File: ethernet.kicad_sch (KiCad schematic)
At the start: 57 parts, among them J4 Bus_RJ45_7499111121A, U9 KSZ9031RNXCA, Y1 Oscillator_SMD_25MHz_KX-7

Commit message: [#65754] Rev 2.0.0 Initial commit - source design files from so-dimm-ddr5-tester e0a54f86
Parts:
- removed C129: C_100n_16V_0402, data-center-rdimm-ddr5-tester-footprints:C_0402_1005Metric, symbol data-center-rdimm-ddr5-tester:C_100n_16V_0402
- removed C146, C147: C_22p_0402, data-center-rdimm-ddr5-tester-footprints:C_0402_1005Metric, symbol data-center-rdimm-ddr5-tester:C_22p_0402
- removed FB1, FB2, FB3, FB4: FB_120Z_2A_0603, data-center-rdimm-ddr5-tester-footprints:FB_0603_1608Metric, symbol data-center-rdimm-ddr5-tester:FB_120Z_2A_Murata-BLM18PG_0603
- removed J4: Bus_RJ45_7499111121A, data-center-rdimm-ddr5-tester-footprints:RJ45_7499111121A_Horizontal, symbol data-center-rdimm-ddr5-tester:Bus_RJ45_7499111121A
- removed R62, R63, R64, R65, R66, R67, R68, R69, R70, R72: R_10k2_0402, data-center-rdimm-ddr5-tester-footprints:R_0402_1005Metric, symbol data-center-rdimm-ddr5-tester:R_10k2_0402
- removed Y1: Oscillator_SMD_25MHz_KX-7, data-center-rdimm-ddr5-tester-footprints:Oscillator_SMD_Geyer_KX-7-4Pin_3.2x2.5mm, symbol data-center-rdimm-ddr5-tester:Oscillator_SMD_25MHz_KX-7
- added C135, C137, C157, C160, C161, C234: C_100n_0402, antmicro-footprints:C_0402_1005Metric, symbol antmicroCapacitors0402:C_100n_0402
- added C162, C163: C_18p_0402, antmicro-footprints:C_0402_1005Metric, symbol antmicroCapacitors0402:C_18p_0402
- added FB4, FB5, FB6: FB_120Z_2A_Murata-BLM18PG_0603, antmicro-footprints:FB_0603_1608Metric, symbol antmicroFerriteBeadsandChips:FB_120Z_2A_Murata-BLM18PG_0603
- added J6: Bus_RJ45_5-2337992-8, antmicro-footprints:RJ45_X-2337992-8_Horizontal, symbol antmicroModularConnectorsJacksWithMagnetics:Bus_RJ45_5-2337992-8
- added R101, R102, R103, R104, R105, R106, R107, R108, R109, R111: R_10k_0402, antmicro-footprints:R_0402_1005Metric, symbol antmicroResistors0402:R_10k_0402
- added R193: R_330R_0402, antmicro-footprints:R_0402_1005Metric, symbol antmicroResistors0402:R_330R_0402
- added Y2: Resonator_25MHz_ABM8G, antmicro-footprints:Resonator_SMD_Abracon_ABM8G_3.2x2.5mm, symbol antmicroResonators:Resonator_25MHz_ABM8G
- C134: renamed from C127; footprint data-center-rdimm-ddr5-tester-footprints:C_0402_1005Metric -> antmicro-footprints:C_0402_1005Metric; symbol data-center-rdimm-ddr5-tester:C_4u7_0402 -> antmicroCapacitors0402:C_4u7_0402
- C136: renamed from C143; footprint data-center-rdimm-ddr5-tester-footprints:C_0402_1005Metric -> antmicro-footprints:C_0402_1005Metric; symbol data-center-rdimm-ddr5-tester:C_10n_0402 -> antmicroCapacitors0402:C_10n_0402
- C138: renamed from C132; footprint data-center-rdimm-ddr5-tester-footprints:C_0402_1005Metric -> antmicro-footprints:C_0402_1005Metric; symbol data-center-rdimm-ddr5-tester:C_470n_0402 -> antmicroCapacitors0402:C_470n_0402
- C139: renamed from C122; footprint data-center-rdimm-ddr5-tester-footprints:C_0402_1005Metric -> antmicro-footprints:C_0402_1005Metric; symbol data-center-rdimm-ddr5-tester:C_4u7_0402 -> antmicroCapacitors0402:C_4u7_0402
- C140: footprint data-center-rdimm-ddr5-tester-footprints:C_0402_1005Metric -> antmicro-footprints:C_0402_1005Metric; symbol data-center-rdimm-ddr5-tester:C_10n_0402 -> antmicroCapacitors0402:C_10n_0402
- C141: renamed from C137; footprint data-center-rdimm-ddr5-tester-footprints:C_0402_1005Metric -> antmicro-footprints:C_0402_1005Metric; symbol data-center-rdimm-ddr5-tester:C_10n_0402 -> antmicroCapacitors0402:C_10n_0402
- C142: renamed from C123; footprint data-center-rdimm-ddr5-tester-footprints:C_0402_1005Metric -> antmicro-footprints:C_0402_1005Metric; symbol data-center-rdimm-ddr5-tester:C_470n_0402 -> antmicroCapacitors0402:C_470n_0402
- C143: renamed from C136; footprint data-center-rdimm-ddr5-tester-footprints:C_0402_1005Metric -> antmicro-footprints:C_0402_1005Metric; symbol data-center-rdimm-ddr5-tester:C_470n_0402 -> antmicroCapacitors0402:C_470n_0402
- C144: renamed from C141; footprint data-center-rdimm-ddr5-tester-footprints:C_0402_1005Metric -> antmicro-footprints:C_0402_1005Metric; symbol data-center-rdimm-ddr5-tester:C_10n_0402 -> antmicroCapacitors0402:C_10n_0402
- C145: renamed from C124; footprint data-center-rdimm-ddr5-tester-footprints:C_0402_1005Metric -> antmicro-footprints:C_0402_1005Metric; symbol data-center-rdimm-ddr5-tester:C_470n_0402 -> antmicroCapacitors0402:C_470n_0402
- C146: renamed from C131; footprint data-center-rdimm-ddr5-tester-footprints:C_0402_1005Metric -> antmicro-footprints:C_0402_1005Metric; symbol data-center-rdimm-ddr5-tester:C_4u7_0402 -> antmicroCapacitors0402:C_4u7_0402
- C147: renamed from C144; footprint data-center-rdimm-ddr5-tester-footprints:C_0402_1005Metric -> antmicro-footprints:C_0402_1005Metric; symbol data-center-rdimm-ddr5-tester:C_10n_0402 -> antmicroCapacitors0402:C_10n_0402
- C148: renamed from C126; footprint data-center-rdimm-ddr5-tester-footprints:C_0402_1005Metric -> antmicro-footprints:C_0402_1005Metric; symbol data-center-rdimm-ddr5-tester:C_470n_0402 -> antmicroCapacitors0402:C_470n_0402
- C149: renamed from C130; footprint data-center-rdimm-ddr5-tester-footprints:C_0402_1005Metric -> antmicro-footprints:C_0402_1005Metric; symbol data-center-rdimm-ddr5-tester:C_470n_0402 -> antmicroCapacitors0402:C_470n_0402
- C150: renamed from C135; footprint data-center-rdimm-ddr5-tester-footprints:C_0402_1005Metric -> antmicro-footprints:C_0402_1005Metric; symbol data-center-rdimm-ddr5-tester:C_10n_0402 -> antmicroCapacitors0402:C_10n_0402
- C151: renamed from C139; footprint data-center-rdimm-ddr5-tester-footprints:C_0402_1005Metric -> antmicro-footprints:C_0402_1005Metric; symbol data-center-rdimm-ddr5-tester:C_10n_0402 -> antmicroCapacitors0402:C_10n_0402
- C152: renamed from C128; footprint data-center-rdimm-ddr5-tester-footprints:C_0402_1005Metric -> antmicro-footprints:C_0402_1005Metric; symbol data-center-rdimm-ddr5-tester:C_4u7_0402 -> antmicroCapacitors0402:C_4u7_0402
- C153: renamed from C142; footprint data-center-rdimm-ddr5-tester-footprints:C_0402_1005Metric -> antmicro-footprints:C_0402_1005Metric; symbol data-center-rdimm-ddr5-tester:C_10n_0402 -> antmicroCapacitors0402:C_10n_0402
- C154: renamed from C134; footprint data-center-rdimm-ddr5-tester-footprints:C_0402_1005Metric -> antmicro-footprints:C_0402_1005Metric; symbol data-center-rdimm-ddr5-tester:C_10n_0402 -> antmicroCapacitors0402:C_10n_0402
- C155: renamed from C133; footprint data-center-rdimm-ddr5-tester-footprints:C_0402_1005Metric -> antmicro-footprints:C_0402_1005Metric; symbol data-center-rdimm-ddr5-tester:C_4u7_0402 -> antmicroCapacitors0402:C_4u7_0402
- C156: renamed from C145; footprint data-center-rdimm-ddr5-tester-footprints:C_0402_1005Metric -> antmicro-footprints:C_0402_1005Metric; symbol data-center-rdimm-ddr5-tester:C_10n_0402 -> antmicroCapacitors0402:C_10n_0402
- C158: renamed from C138; footprint data-center-rdimm-ddr5-tester-footprints:C_0402_1005Metric -> antmicro-footprints:C_0402_1005Metric; symbol data-center-rdimm-ddr5-tester:C_4u7_0402 -> antmicroCapacitors0402:C_4u7_0402
- C159: renamed from C125; footprint data-center-rdimm-ddr5-tester-footprints:C_0402_1005Metric -> antmicro-footprints:C_0402_1005Metric; symbol data-center-rdimm-ddr5-tester:C_4u7_0402 -> antmicroCapacitors0402:C_4u7_0402
- R100: renamed from R61; footprint data-center-rdimm-ddr5-tester-footprints:R_0402_1005Metric -> antmicro-footprints:R_0402_1005Metric; symbol data-center-rdimm-ddr5-tester:R_1M8_0402 -> antmicroResistors0402:R_1M8_0402
- R110: renamed from R71; footprint data-center-rdimm-ddr5-tester-footprints:R_0402_1005Metric -> antmicro-footprints:R_0402_1005Metric; symbol data-center-rdimm-ddr5-tester:R_1k_0402 -> antmicroResistors0402:R_1k_0402
- R112: renamed from R59; footprint data-center-rdimm-ddr5-tester-footprints:R_0402_1005Metric -> antmicro-footprints:R_0402_1005Metric; symbol data-center-rdimm-ddr5-tester:R_12k1_0402 -> antmicroResistors0402:R_12k1_0402
- R113: renamed from R73; footprint data-center-rdimm-ddr5-tester-footprints:R_0402_1005Metric -> antmicro-footprints:R_0402_1005Metric; symbol data-center-rdimm-ddr5-tester:R_2k2_0402 -> antmicroResistors0402:R_2k2_0402
- R114: renamed from R74; footprint data-center-rdimm-ddr5-tester-footprints:R_0402_1005Metric -> antmicro-footprints:R_0402_1005Metric; symbol data-center-rdimm-ddr5-tester:R_2k2_0402 -> antmicroResistors0402:R_2k2_0402
- R115: renamed from R75; footprint data-center-rdimm-ddr5-tester-footprints:R_0402_1005Metric -> antmicro-footprints:R_0402_1005Metric; symbol data-center-rdimm-ddr5-tester:R_2k2_0402 -> antmicroResistors0402:R_2k2_0402
- R116: renamed from R76; footprint data-center-rdimm-ddr5-tester-footprints:R_0402_1005Metric -> antmicro-footprints:R_0402_1005Metric; symbol data-center-rdimm-ddr5-tester:R_2k2_0402 -> antmicroResistors0402:R_2k2_0402
- R117: renamed from R77; footprint data-center-rdimm-ddr5-tester-footprints:R_0402_1005Metric -> antmicro-footprints:R_0402_1005Metric; symbol data-center-rdimm-ddr5-tester:R_2k2_0402 -> antmicroResistors0402:R_2k2_0402
- R118: renamed from R78; footprint data-center-rdimm-ddr5-tester-footprints:R_0402_1005Metric -> antmicro-footprints:R_0402_1005Metric; symbol data-center-rdimm-ddr5-tester:R_2k2_0402 -> antmicroResistors0402:R_2k2_0402
- R119: renamed from R79; footprint data-center-rdimm-ddr5-tester-footprints:R_0402_1005Metric -> antmicro-footprints:R_0402_1005Metric; symbol data-center-rdimm-ddr5-tester:R_2k2_0402 -> antmicroResistors0402:R_2k2_0402
- R120: renamed from R80; footprint data-center-rdimm-ddr5-tester-footprints:R_0402_1005Metric -> antmicro-footprints:R_0402_1005Metric; symbol data-center-rdimm-ddr5-tester:R_2k2_0402 -> antmicroResistors0402:R_2k2_0402
- R121: renamed from R81; footprint data-center-rdimm-ddr5-tester-footprints:R_0402_1005Metric -> antmicro-footprints:R_0402_1005Metric; symbol data-center-rdimm-ddr5-tester:R_2k2_0402 -> antmicroResistors0402:R_2k2_0402
- R98: renamed from R58; footprint data-center-rdimm-ddr5-tester-footprints:R_0402_1005Metric -> antmicro-footprints:R_0402_1005Metric; symbol data-center-rdimm-ddr5-tester:R_220R_0402 -> antmicroResistors0402:R_220R_0402
- R99: renamed from R60; footprint data-center-rdimm-ddr5-tester-footprints:R_0402_1005Metric -> antmicro-footprints:R_0402_1005Metric; symbol data-center-rdimm-ddr5-tester:R_220R_0402 -> antmicroResistors0402:R_220R_0402
- U15: renamed from U9; footprint data-center-rdimm-ddr5-tester-footprints:QFN-48-1EP_7x7x0.9mm_P0.5mm_EP3.5x3.5mm -> antmicro-footprints:QFN-48-1EP_7x7x0.9mm_P0.5mm_EP3.5x3.5mm; symbol data-center-rdimm-ddr5-tester:KSZ9031RNXCA -> antmicroInterfaceControllers:KSZ9031RNXCA
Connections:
- net AVDDH: now also FB5.2
- net AVDDL: now also FB4.2
- net AVDDL_PLL: now also C157.2, FB6.2
- net ETH1_N: now also J6.2 (P2)
- net ETH1_P: now also J6.1 (P1)
- net ETH2_N: now also J6.6 (P6)
- net ETH2_P: now also J6.3 (P3)
- net ETH3_N: now also J6.8 (P8)
- net ETH3_P: now also J6.7 (P7)
- net ETH4_N: now also J6.10 (P10)
- net ETH4_P: now also J6.9 (P9)
- net GND: now also R112.1, C135.1, C137.1, C157.1, C160.1, C161.1, C162.1, C163.1, C234.2, R193.1, Y2.2 (SH), Y2.4 (SH); no longer R112.2
- net LED_LINK: now also J6.18 (LED_YEL-), R109.1
- net LED_SPD: now also J6.16 (LED_GRN-), R108.1
- net at R100.1, U15.45 (XO): now also C163.2, Y2.1
- net at R100.2, U15.46 (XI): now also C162.2, Y2.3
- net at U15.48 (ISET): now also R112.2; no longer R112.1
- net at R98.1: now also J6.17 (LED_YEL+)
- net at R99.1: now also J6.15 (LED_GRN+)
- net 1V2_SYS renamed +1V2
- net +1V2: now also FB4.1, FB6.1
- net 3V3_SYS renamed +3V3
- net +3V3: now also C160.2, C161.2, FB5.1, R101.2, R102.2, R103.2, R104.2, R105.2, R106.2, R107.2, R108.2, R109.2, R111.2
- net ETH_INT_N renamed ETH.~{INT}
- net ETH_MDC renamed ETH.MDC
- net ETH_MDIO renamed ETH.MDIO
- net ETH_REF_CLK renamed ETH.REF_CLK
- net ETH.REF_CLK: now also R107.1
- net ETH_RSTN renamed ETH.~{RESET}
- net ETH.~{RESET}: now also R111.1
- net ETH_RXD0 renamed ETH.RXD0
- net ETH.RXD0: now also R101.1
- net ETH_RXD1 renamed ETH.RXD1
- net ETH.RXD1: now also R102.1
- net ETH_RXD2 renamed ETH.RXD2
- net ETH.RXD2: now also R103.1
- net ETH_RXD3 renamed ETH.RXD3
- net ETH.RXD3: now also R104.1
- net ETH_RX_CLK renamed ETH.RXC
- net ETH.RXC: now also R106.1
- net ETH_RX_DV renamed ETH.RX_CTL
- net ETH.RX_CTL: now also R105.1
- net ETH_TXD0 renamed ETH.TXD0
- net ETH_TXD1 renamed ETH.TXD1
- net ETH_TXD2 renamed ETH.TXD2
- net ETH_TXD3 renamed ETH.TXD3
- net ETH_TX_CLK renamed ETH.TXC
- net ETH_TX_EN renamed ETH.TX_CTL
- new net: C135.2, J6.4 (P4)
- new net: C137.2, J6.5 (P5)
- new net: C234.1, J6.19 (SHIELD), J6.20 (SHIELD), R193.2
- no-connect marks 2 -> 5
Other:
- note added: "Bootstrap configuration"
- note added: "CLK125_EN"
- note added: "Gigabit Ethernet"
- note added: "LED_MODE"
- note added: "MODE0"
- note added: "MODE1"
- note added: "MODE2"
- note added: "MODE3"
- note added: "MODE[3:0] : 1100 (RGMII mode - Advertise 1000BASE-T full-duplex only) PHYAD[4:0]: 00011 CLK125_EN: 0, disabled LED_MODE: 1, Single-LED mode"
- note added: "PHYAD0"
- note added: "PHYAD1"
- note added: "PHYAD2"
- note added: "Reference plane decoupling"
- note removed: "AVDDH decoupling"
- note removed: "AVDDL decoupling"
- note removed: "AVDDL_PLL decoupling"
- note removed: "DVDDH decoupling"
- note removed: "DVDDL decoupling"
- note removed: "PHY"
- note removed: "Pull down resistors"
- note removed: "Pull up resistors"
- note removed: "RJ45 Connector"
- title: Data Center RDIMM DDR5 Tester -> SO-DIMM DDR5 Tester
- moved on the sheet: C134, C136, C138, C139, C140, C141, C142, C143, C144, C145, C146, C147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

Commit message: [#65754] Rename project
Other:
- title: SO-DIMM DDR5 Tester -> RDIMM DDR5 Tester

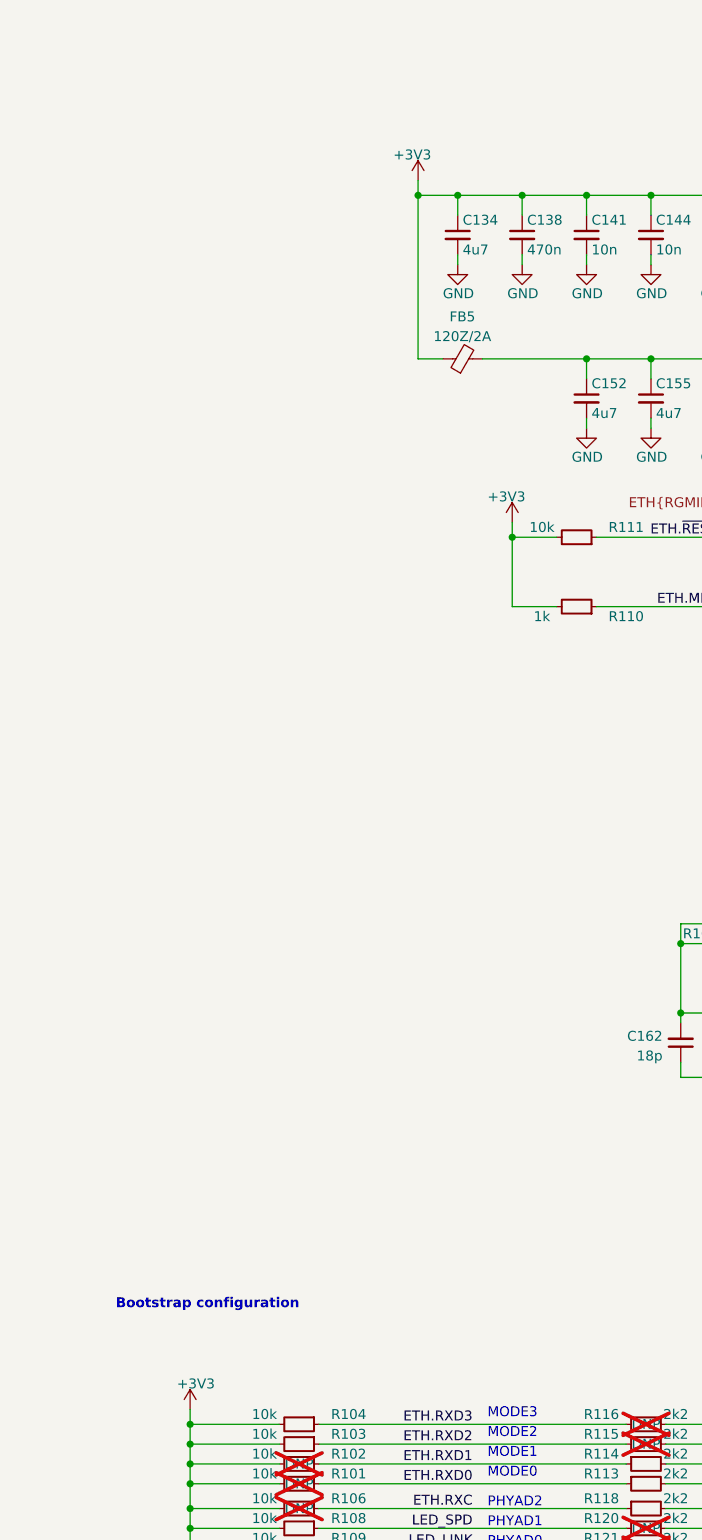
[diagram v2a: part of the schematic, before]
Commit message: [#66727] Reconfigure ETH PHY IO voltage to 1V8
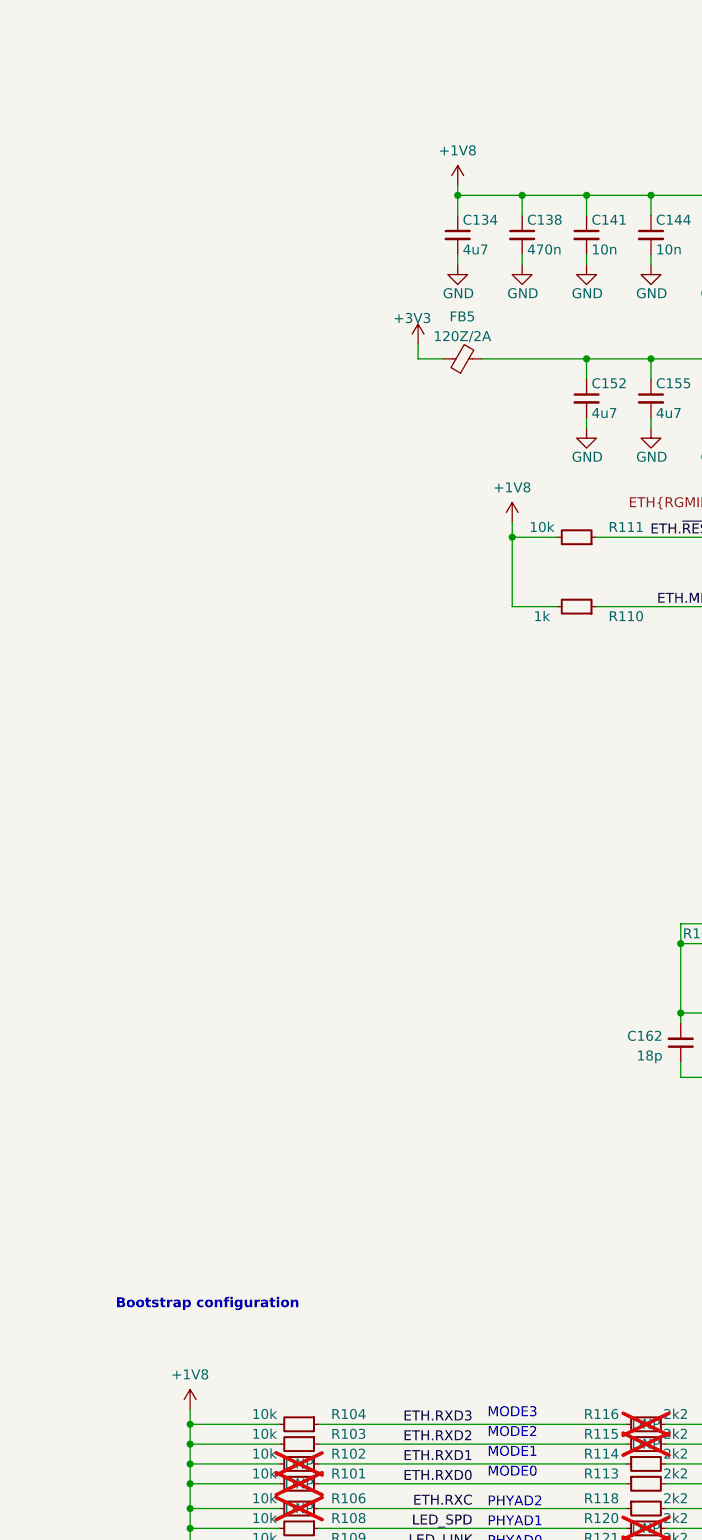
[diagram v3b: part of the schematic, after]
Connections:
- net +3V3: no longer C134.1, C138.1, C141.1, C144.1, C147.1, R101.2, R102.2, R103.2, R104.2, R105.2, R106.2, R107.2, R108.2, R109.2, R110.2, R111.2, U15.16 (DVDDH), U15.34 (DVDDH), U15.40 (DVDDH)
- new net +1V8: C134.1, C138.1, C141.1, C144.1, C147.1, R101.2, R102.2, R103.2, R104.2, R105.2, R106.2, R107.2, R108.2, R109.2, R110.2, R111.2, U15.16 (DVDDH), U15.34 (DVDDH), U15.40 (DVDDH)
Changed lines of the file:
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@@
   (junction (at 45.085 208.915) (diameter 0) (color 0 0 0 0)
   )
-  (junction (at 79.375 48.895) (diameter 0) (color 0 0 0 0)
-  )
   (junction (at 45.085 211.455) (diameter 0) (color 0 0 0 0)
   )
@@
   (junction (at 114.935 161.925) (diameter 0) (color 0 0 0 0)
   )
+  (junction (at 79.375 48.895) (diameter 0) (color 0 0 0 0)
+  )
   (junction (at 190.5 53.975) (diameter 0) (color 0 0 0 0)
   )
@@
   (junction (at 45.085 225.425) (diameter 0) (color 0 0 0 0)
   )
-  (junction (at 74.295 48.895) (diameter 0) (color 0 0 0 0)
-  )
   (junction (at 45.085 206.375) (diameter 0) (color 0 0 0 0)
   )
@@
     (stroke (width 0) (type default))
   )
-  (wire (pts (xy 74.295 69.85) (xy 74.295 48.895))
-    (stroke (width 0) (type default))
-  )
   (wire (pts (xy 56.515 208.915) (xy 45.085 208.915))
     (stroke (width 0) (type default))
@@
     (stroke (width 0) (type default))
   )
+  (wire (pts (xy 79.375 47.625) (xy 79.375 48.895))
+    (stroke (width 0) (type default))
+  )
   (wire (pts (xy 198.755 82.55) (xy 198.755 83.82))
     (stroke (width 0) (type default))
@@
     (stroke (width 0) (type default))
   )
-  (wire (pts (xy 74.295 46.99) (xy 74.295 48.895))
+  (wire (pts (xy 74.295 67.945) (xy 74.295 69.85))
     (stroke (width 0) (type default))
   )
@@
     (stroke (width 0) (type default))
   )
-  (wire (pts (xy 74.295 48.895) (xy 79.375 48.895))
-    (stroke (width 0) (type default))
-  )
   (wire (pts (xy 107.95 144.78) (xy 112.395 144.78))
     (stroke (width 0) (type default))
@@
     )
   )
+  (symbol (lib_id "antmicropower:+1V8") (at 86.36 90.805 0) (unit 1)
+    (in_bom yes) (on_board yes) (dnp no) (fields_autoplaced)
+    (property "Reference" "#PWR0238" (at 101.6 93.345 0)
+      (effects (font (size 1.27 1.27) (thickness 0.15)) (justify left bottom) hide)
+    )
+    (property "Value" "+1V8" (at 86.36 86.36 0)
+      (effects (font (size 1.27 1.27) (thickness 0.15)))
+    )
+    (property "Footprint" "" (at 101.6 98.425 0)
+      (effects (font (size 1.27 1.27) (thickness 0.15)) (justify left bottom) hide)
+    )
+    (property "Datasheet" "" (at 101.6 100.965 0)
+      (effects (font (size 1.27 1.27) (thickness 0.15)) (justify left bottom) hide)
+    )
+    (property "Author" "Antmicro" (at 101.6 95.885 0)
+      (effects (font (size 1.27 1.27) (thickness 0.15)) (justify left bottom) hide)
+    )
+    (property "License" "Apache-2.0" (at 101.6 98.425 0)
+      (effects (font (size 1.27 1.27) (thickness 0.15)) (justify left bottom) hide)
+    )
+    (pin "1")
+    (instances
+      (project "data-center-rdimm-ddr5-tester"
+        (path "/1faa6543-e26a-4449-8bac-ee14b9f19e5f/00000000-0000-0000-0000-00005f982999"
+          (reference "#PWR0238") (unit 1)
+        )
+      )
+    )
+  )
   (symbol (lib_id "antmicroResistors0402:R_10k_0402") (at 61.595 225.425 0) (mirror y) (unit 1)
     (in_bom no) (on_board yes) (dnp yes)
@@
     )
   )
-  (symbol (lib_id "antmicropower:+3V3") (at 45.085 204.47 0) (mirror y) (unit 1)
-    (in_bom yes) (on_board yes) (dnp no)
-    (property "Reference" "#PWR0258" (at 45.085 208.28 0)
-      (effects (font (size 1.27 1.27)) hide)
-    )
-    (property "Value" "+3V3" (at 48.26 201.93 0)
-      (effects (font (size 1.27 1.27) (thickness 0.15)) (justify left bottom))
-    )
-    (property "Footprint" "" (at 29.845 212.09 0)
-      (effects (font (size 1.27 1.27) (thickness 0.15)) (justify left bottom) hide)
-    )
-    (property "Datasheet" "" (at 29.845 214.63 0)
-      (effects (font (size 1.27 1.27) (thickness 0.15)) (justify left bottom) hide)
-    )
-    (property "Author" "Antmicro" (at 29.845 207.01 0)
-      (effects (font (size 1.27 1.27) (thickness 0.15)) (justify left bottom) hide)
-    )
-    (property "License" "Apache-2.0" (at 29.845 209.55 0)
-      (effects (font (size 1.27 1.27) (thickness 0.15)) (justify left bottom) hide)
-    )
-    (pin "1")
-    (instances
-      (project "data-center-rdimm-ddr5-tester"
-        (path "/1faa6543-e26a-4449-8bac-ee14b9f19e5f/00000000-0000-0000-0000-00005f982999"
-          (reference "#PWR0258") (unit 1)
-        )
-      )
-    )
-  )
   (symbol (lib_id "antmicropower:PWR_FLAG") (at 243.84 75.565 0) (unit 1)
     (in_bom yes) (on_board yes) (dnp no) (fields_autoplaced)
@@
     )
   )
+  (symbol (lib_id "antmicropower:+1V8") (at 45.085 204.47 0) (unit 1)
+    (in_bom yes) (on_board yes) (dnp no) (fields_autoplaced)
+    (property "Reference" "#PWR0258" (at 60.325 207.01 0)
+      (effects (font (size 1.27 1.27) (thickness 0.15)) (justify left bottom) hide)
+    )
+    (property "Value" "+1V8" (at 45.085 200.025 0)
+      (effects (font (size 1.27 1.27) (thickness 0.15)))
+    )
+    (property "Footprint" "" (at 60.325 212.09 0)
+      (effects (font (size 1.27 1.27) (thickness 0.15)) (justify left bottom) hide)
+    )
+    (property "Datasheet" "" (at 60.325 214.63 0)
+      (effects (font (size 1.27 1.27) (thickness 0.15)) (justify left bottom) hide)
+    )
+    (property "Author" "Antmicro" (at 60.325 209.55 0)
+      (effects (font (size 1.27 1.27) (thickness 0.15)) (justify left bottom) hide)
+    )
+    (property "License" "Apache-2.0" (at 60.325 212.09 0)
+      (effects (font (size 1.27 1.27) (thickness 0.15)) (justify left bottom) hide)
+    )
+    (pin "1")
+    (instances
+      (project "data-center-rdimm-ddr5-tester"
+        (path "/1faa6543-e26a-4449-8bac-ee14b9f19e5f/00000000-0000-0000-0000-00005f982999"
+          (reference "#PWR0258") (unit 1)
+        )
+      )
+    )
+  )
   (symbol (lib_id "antmicropower:GND") (at 190.5 83.82 0) (unit 1)
     (in_bom yes) (on_board yes) (dnp no) (fields_autoplaced)
@@
     )
   )
-  (symbol (lib_id "antmicropower:+3V3") (at 74.295 46.99 0) (unit 1)
+  (symbol (lib_id "antmicropower:+3V3") (at 74.295 67.945 0) (unit 1)
     (in_bom yes) (on_board yes) (dnp no) (fields_autoplaced)
-    (property "Reference" "#PWR0240" (at 74.295 50.8 0)
+    (property "Reference" "#PWR0240" (at 74.295 71.755 0)
       (effects (font (size 1.27 1.27)) hide)
     )
-    (property "Value" "+3V3" (at 71.12 44.45 0)
+    (property "Value" "+3V3" (at 71.12 65.405 0)
       (effects (font (size 1.27 1.27) (thickness 0.15)) (justify left bottom))
     )
-    (property "Footprint" "" (at 89.535 54.61 0)
+    (property "Footprint" "" (at 89.535 75.565 0)
       (effects (font (size 1.27 1.27) (thickness 0.15)) (justify left bottom) hide)
     )
-    (property "Datasheet" "" (at 89.535 57.15 0)
+    (property "Datasheet" "" (at 89.535 78.105 0)
       (effects (font (size 1.27 1.27) (thickness 0.15)) (justify left bottom) hide)
     )
-    (property "Author" "Antmicro" (at 89.535 49.53 0)
+    (property "Author" "Antmicro" (at 89.535 70.485 0)
       (effects (font (size 1.27 1.27) (thickness 0.15)) (justify left bottom) hide)
     )
-    (property "License" "Apache-2.0" (at 89.535 52.07 0)
+    (property "License" "Apache-2.0" (at 89.535 73.025 0)
       (effects (font (size 1.27 1.27) (thickness 0.15)) (justify left bottom) hide)
     )
@@
     )
   )
-  (symbol (lib_id "antmicropower:+3V3") (at 86.36 90.805 0) (unit 1)
+  (symbol (lib_id "antmicropower:+1V8") (at 79.375 47.625 0) (unit 1)
     (in_bom yes) (on_board yes) (dnp no) (fields_autoplaced)
-    (property "Reference" "#PWR0407" (at 86.36 94.615 0)
-      (effects (font (size 1.27 1.27)) hide)
+    (property "Reference" "#PWR0236" (at 94.615 50.165 0)
+      (effects (font (size 1.27 1.27) (thickness 0.15)) (justify left bottom) hide)
     )
-    (property "Value" "+3V3" (at 83.185 88.265 0)
-      (effects (font (size 1.27 1.27) (thickness 0.15)) (justify left bottom))
+    (property "Value" "+1V8" (at 79.375 43.18 0)
+      (effects (font (size 1.27 1.27) (thickness 0.15)))
     )
-    (property "Footprint" "" (at 101.6 98.425 0)
+    (property "Footprint" "" (at 94.615 55.245 0)
       (effects (font (size 1.27 1.27) (thickness 0.15)) (justify left bottom) hide)
     )
-    (property "Datasheet" "" (at 101.6 100.965 0)
+    (property "Datasheet" "" (at 94.615 57.785 0)
       (effects (font (size 1.27 1.27) (thickness 0.15)) (justify left bottom) hide)
     )
-    (property "Author" "Antmicro" (at 101.6 93.345 0)
+    (property "Author" "Antmicro" (at 94.615 52.705 0)
       (effects (font (size 1.27 1.27) (thickness 0.15)) (justify left bottom) hide)
     )
-    (property "License" "Apache-2.0" (at 101.6 95.885 0)
+    (property "License" "Apache-2.0" (at 94.615 55.245 0)
       (effects (font (size 1.27 1.27) (thickness 0.15)) (justify left bottom) hide)
     )
@@
       (project "data-center-rdimm-ddr5-tester"
         (path "/1faa6543-e26a-4449-8bac-ee14b9f19e5f/00000000-0000-0000-0000-00005f982999"
-          (reference "#PWR0407") (unit 1)
+          (reference "#PWR0236") (unit 1)
         )
       )
